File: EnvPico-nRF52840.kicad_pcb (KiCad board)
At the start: 2 copper layers, 21.2 x 57.7 mm, 49 parts, among them J3 2.54mm header 01x20, J4 2.54mm header 01x20, J5 Conn_01x03_Male, U1 LM3671MF 3.3, U2 BQ24072RGT, U3 nRF52840, Y1 32MHz 12pF

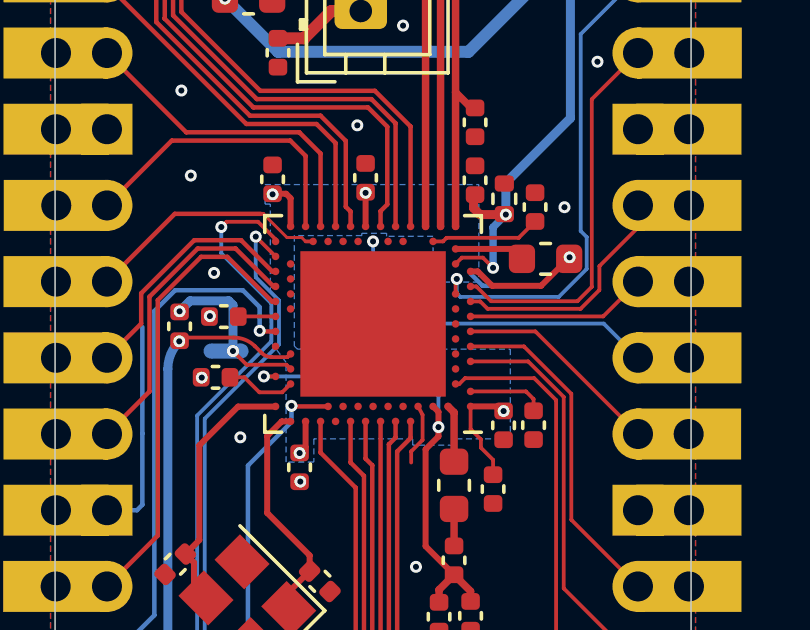
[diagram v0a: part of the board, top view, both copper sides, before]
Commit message: adjusted footprint of nRF52840 a bit, adjusted few traces and via locations.
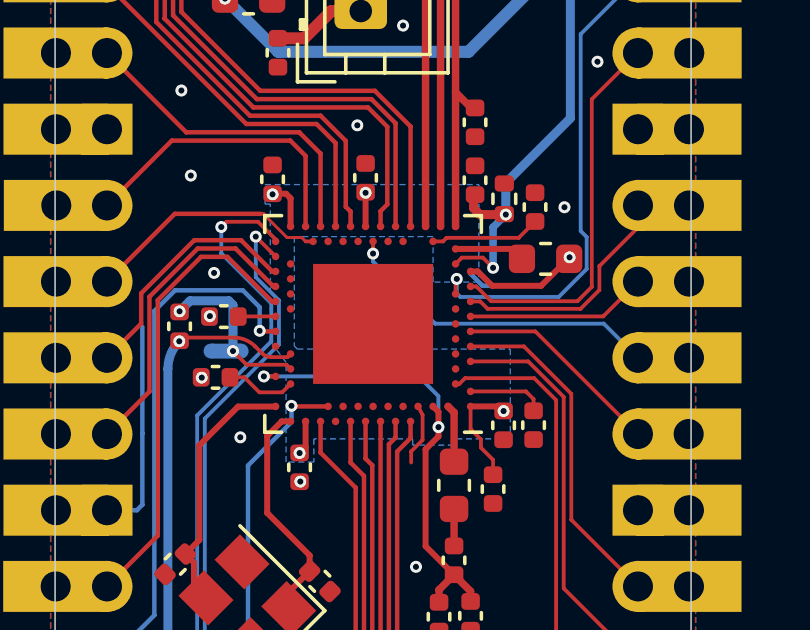
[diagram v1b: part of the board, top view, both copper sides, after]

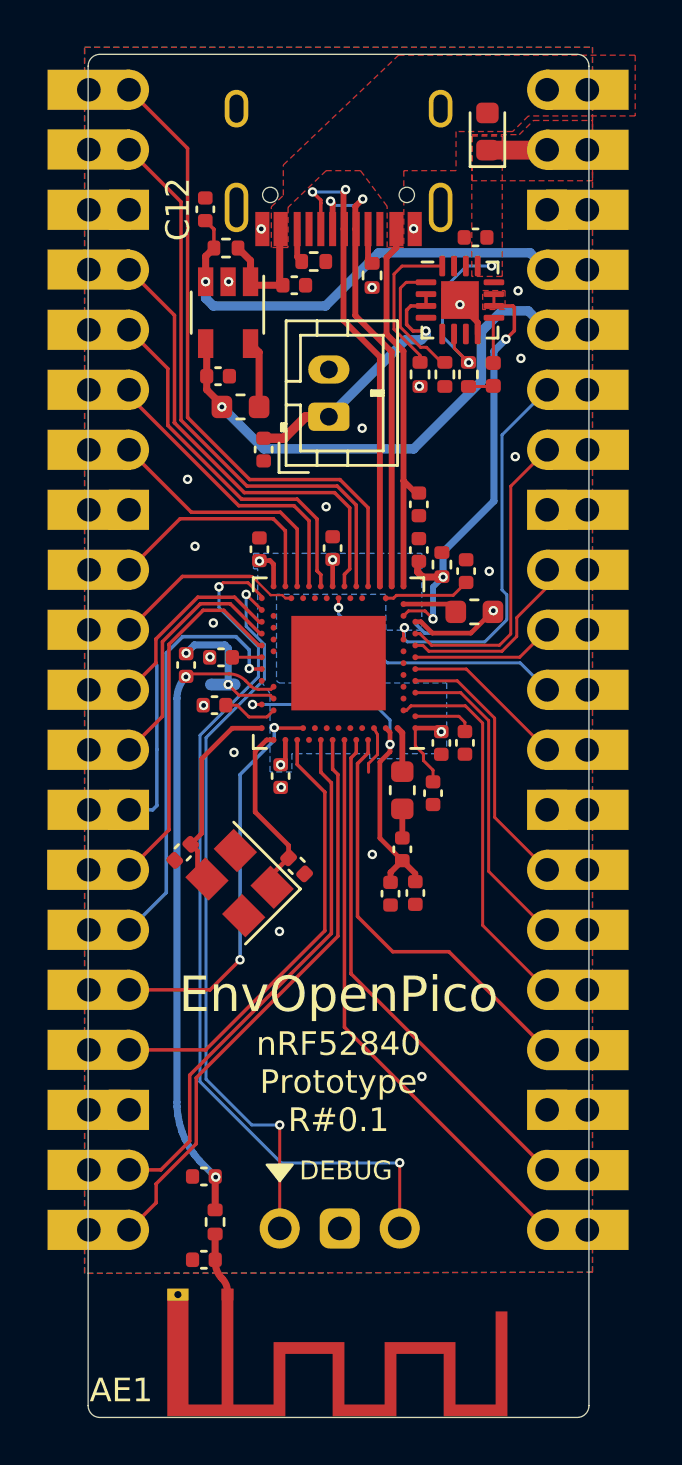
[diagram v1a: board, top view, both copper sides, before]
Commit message: moved some traces about to make sure there is good ground coverage
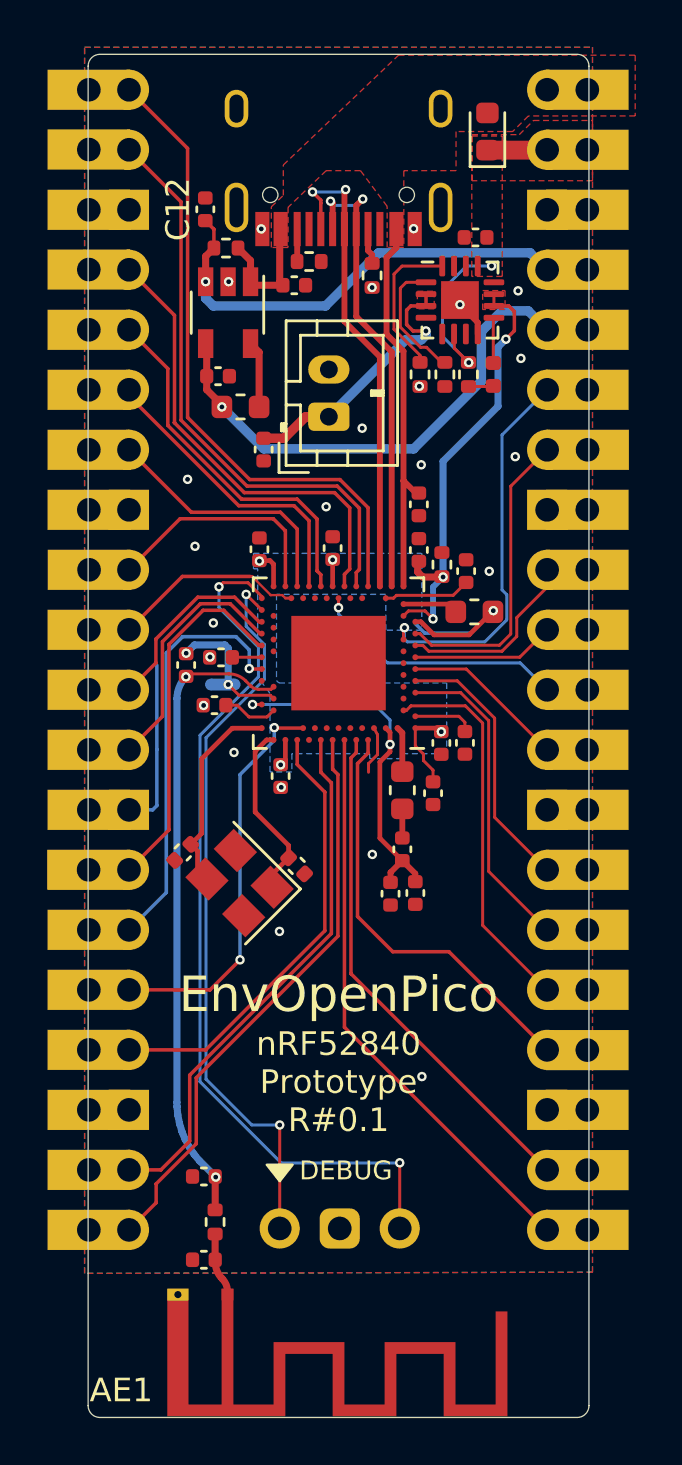
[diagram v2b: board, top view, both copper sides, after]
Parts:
- moved R6 0.19 mm to (102.4, 66.0)
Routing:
- net GND: vias 22 -> 23
- added copper zone on F.Cu, net Net-(BT1-Pad1)

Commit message: fixed leftover silkscreen C12, couple of plane tweaks and added center marker / board dimensions on back of PCB, fixed incorrect diode footprint and in schematic
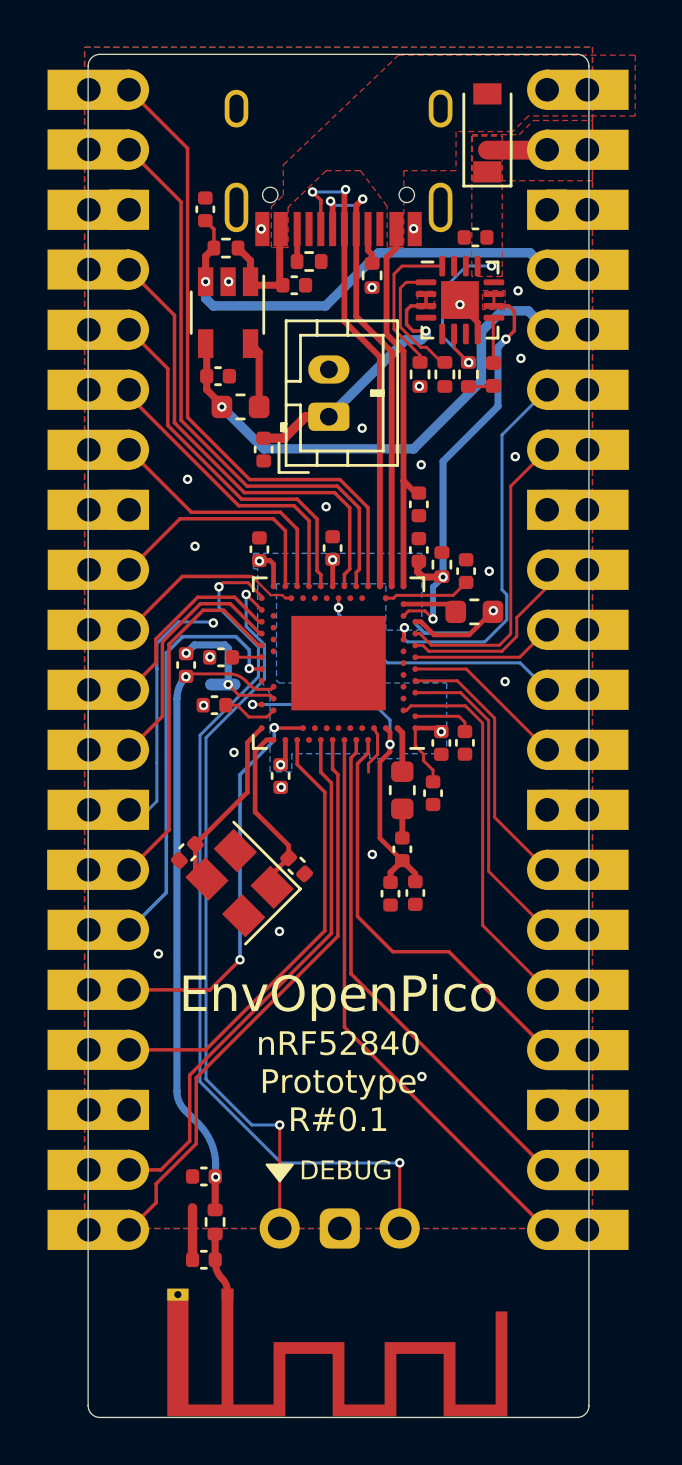
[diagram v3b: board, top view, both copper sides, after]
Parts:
- D4: value Schottky 0603 -> 1N4002W; footprint Diode_SMD:D_0603_1608Metric -> Diode_SMD:D_SOD-123
- moved C10 0.19 mm to (97.2, 91.0)
- moved D4 0.06 mm to (109.9, 60.5)
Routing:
- net GND: track 11.0 -> 16.8 mm, vias 23 -> 25
- net Net-(C10-Pad2): track 8.64 -> 7.75 mm
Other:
- board text added: "21.2mm"
- board text added: "57.7mm"
- board text added: "SWCLK"
- board text added: "SWDIO"

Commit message: some edits and corrections
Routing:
- net GND: track 16.8 -> 20.6 mm, vias 25 -> 26
- net /SWD: track 37.5 -> 35.6 mm
- net /SWCLK: track 31.1 -> 29.2 mm
- net Net-(C23-Pad2): track 16.0 -> 14.2 mm
- net GPIO26: track 16.4 -> 15.4 mm
- net GPIO7: vias 0 -> 2

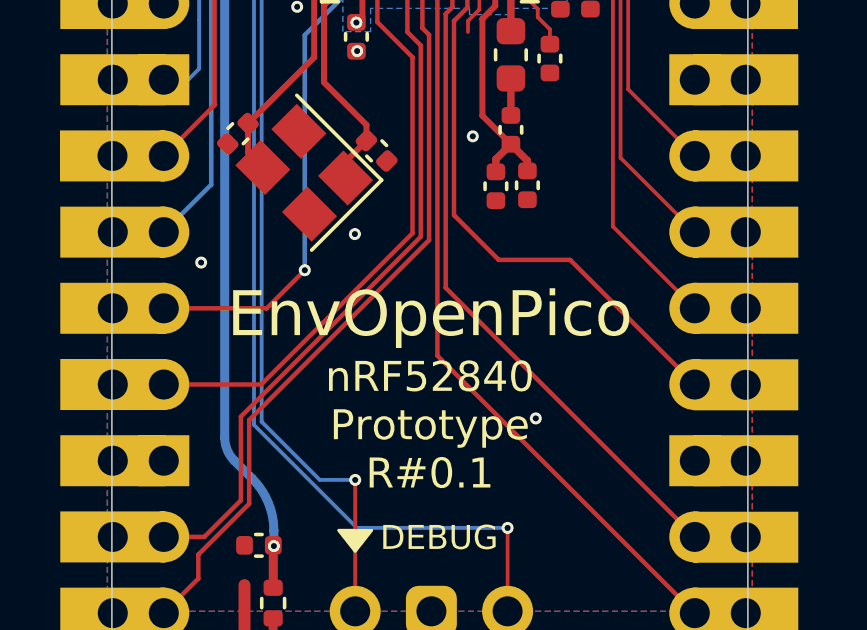
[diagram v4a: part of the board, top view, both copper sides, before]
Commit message: added silkscreen pin labels to the bottom of the PCB
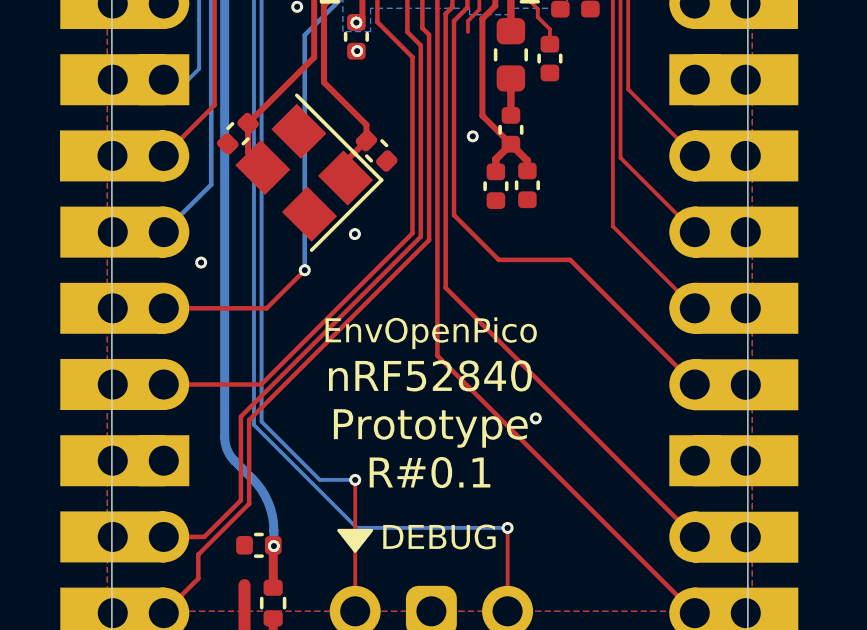
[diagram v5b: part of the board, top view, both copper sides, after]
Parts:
- removed G***: LOGO, EnvExtras:logo
- renumbered e1 to USB1
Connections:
- U2 pad 12: unconnected-(U2-Pad12) -> (no net)
- U2 pad 14: unconnected-(U2-Pad14) -> (no net)
- U2 pad 7: unconnected-(U2-Pad7) -> (no net)
- U3 pad A18: unconnected-(U3-PadA18) -> (no net)
- U3 pad AC11: unconnected-(U3-PadAC11) -> (no net)
- U3 pad AC15: unconnected-(U3-PadAC15) -> (no net)
- U3 pad AC17: unconnected-(U3-PadAC17) -> (no net)
- U3 pad AC19: unconnected-(U3-PadAC19) -> (no net)
- U3 pad AC9: unconnected-(U3-PadAC9) -> (no net)
- U3 pad B11: unconnected-(U3-PadB11) -> (no net)
- U3 pad B13: unconnected-(U3-PadB13) -> (no net)
- U3 pad B15: unconnected-(U3-PadB15) -> (no net)
- U3 pad B17: unconnected-(U3-PadB17) -> (no net)
- U3 pad B9: unconnected-(U3-PadB9) -> (no net)
- U3 pad F2: unconnected-(U3-PadF2) -> (no net)
- U3 pad H2: unconnected-(U3-PadH2) -> (no net)
- U3 pad J24: unconnected-(U3-PadJ24) -> (no net)
- U3 pad K2: unconnected-(U3-PadK2) -> (no net)
- U3 pad M2: unconnected-(U3-PadM2) -> (no net)
- U3 pad P2: unconnected-(U3-PadP2) -> (no net)
- U3 pad P23: unconnected-(U3-PadP23) -> (no net)
- U3 pad T23: unconnected-(U3-PadT23) -> (no net)
- U3 pad V23: unconnected-(U3-PadV23) -> (no net)
- U3 pad Y23: unconnected-(U3-PadY23) -> (no net)
- USB1 pad 3: unconnected-(e1-Pad3) -> (no net)
- USB1 pad 9: unconnected-(e1-Pad9) -> (no net)
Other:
- board text added: "P0.00"
- board text added: "P0.02"
- board text added: "P0.04"
- board text added: "P0.06"
- board text added: "P0.08"
- board text added: "P0.09"
- board text added: "P0.11"
- board text added: "P0.12"
- board text added: "P0.13"
- board text added: "P0.15"
- board text added: "P0.17"
- board text added: "P0.20"
- board text added: "P0.22"
- board text added: "P0.24"
- board text added: "P0.25"
- board text added: "P0.26"
- board text added: "P0.29"
- board text added: "P0.31"
- board text added: "P1.00"
- board text added: "P1.02"
- board text added: "P1.04"
- board text added: "P1.06"
- board text added: "P1.09"
- board text added: "P1.10"
- board text added: "P1.11"
- board text added: "P1.13"
- board text added: "P1.15"
- board text removed: "21.2mm"
- board text removed: "57.7mm"

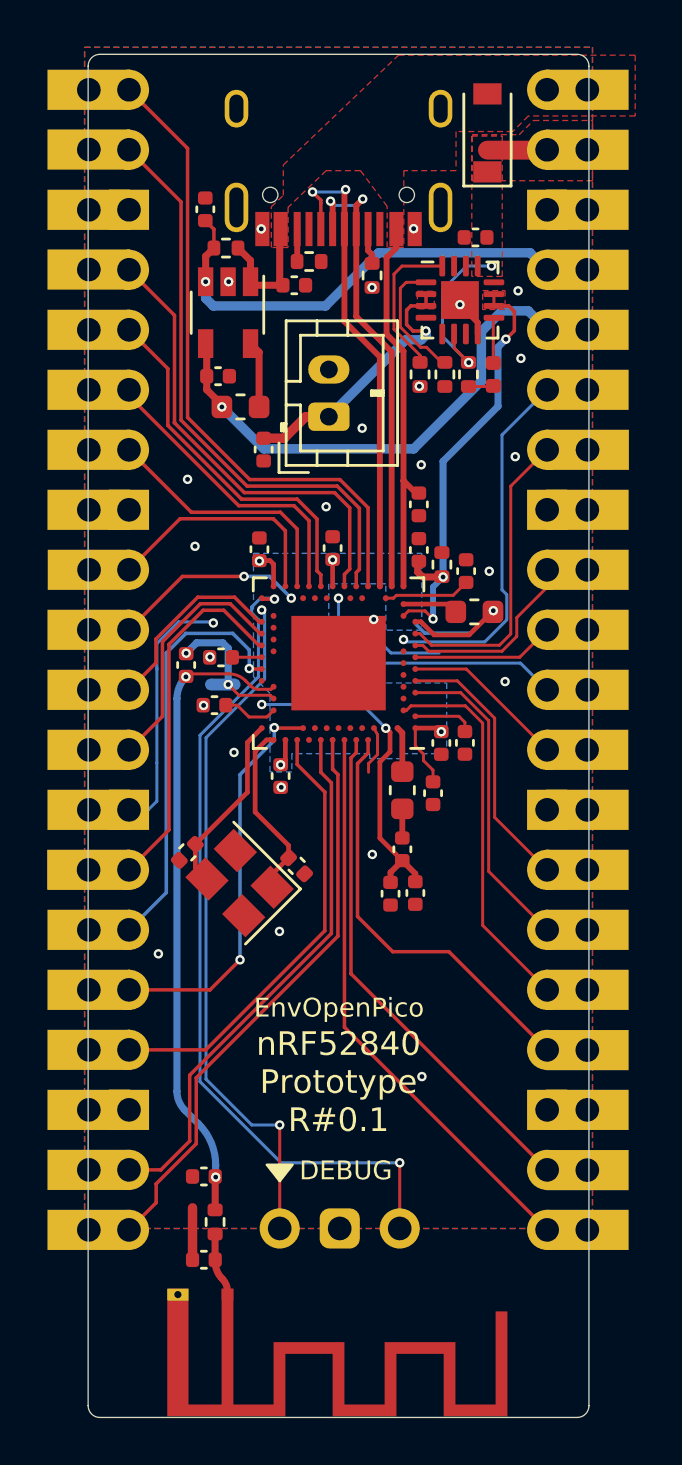
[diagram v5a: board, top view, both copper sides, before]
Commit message: Corrected Antenna stuff hopefully
this is voodoo to me so its probably still wrong.
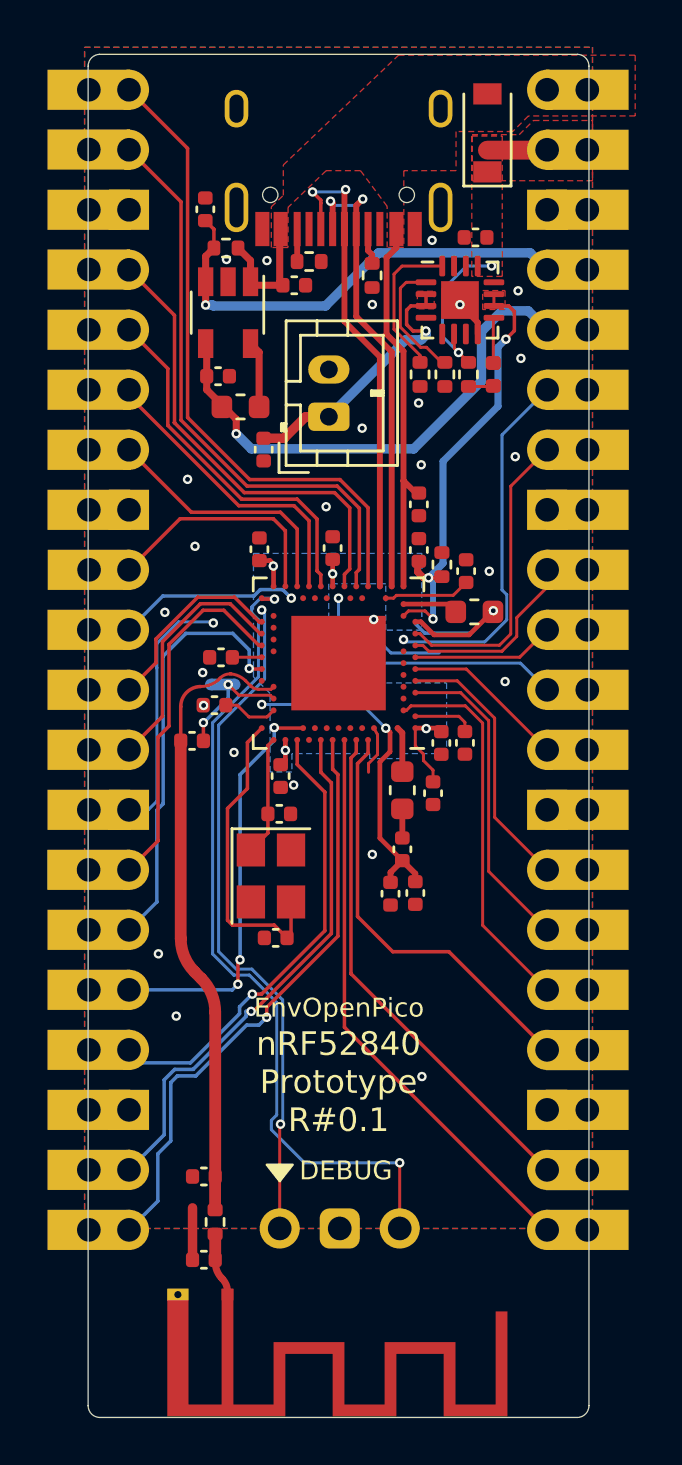
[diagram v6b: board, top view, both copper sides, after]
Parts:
- moved C10 5.20 mm to (101.0, 94.6), turned to 0 degrees
- moved C14 3.22 mm to (97.4, 86.3), turned to 0 degrees
- moved C11 2.32 mm to (101.1, 89.4), turned to 180 degrees
- moved Y1 1.36 mm to (100.8, 92.0), turned to -90 degrees
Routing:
- net Net-(C10-Pad2): track 7.75 -> 13.2 mm
- net Net-(C11-Pad2): track 7.61 -> 5.06 mm
- net GPIO15: track 24.5 -> 25.3 mm, vias 0 -> 1
- net VSS_PA: track 5.76 -> 5.01 mm
- net Net-(C13-Pad1): track 27.2 -> 26.5 mm, vias 2 -> 0
- net /SWCLK: track 29.2 -> 28.6 mm
- net GPIO13: track 18.9 -> 19.6 mm, vias 0 -> 1
- net VSYS: track 9.85 -> 9.25 mm
- net GPIO12: track 16.9 -> 17.4 mm, vias 2 -> 3
- net GPIO7: track 8.19 -> 7.72 mm, vias 2 -> 1
- net GPIO14: track 22.7 -> 22.6 mm, vias 0 -> 1
- net GND: vias 26 -> 27
